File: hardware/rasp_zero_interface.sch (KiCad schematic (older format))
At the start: 0 parts

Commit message: work in progress - components ordered
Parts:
- added J2: Raspberry_Pi_2_3, Speeduino Mini:RaspberryPi_uHAT, symbol Connector:Raspberry_Pi_2_3
- added R23: 150, Resistors_SMD:R_0805, symbol Device:R
- added R24: 10k, Resistors_SMD:R_0805, symbol Device:R
- added U10, U5, U9: SN74LVC2T45-VSSOP, Housings_SSOP:VSSOP-8_2.3x2mm_Pitch0.5mm, symbol speeduino_mini:SN74LVC2T45-VSSOP
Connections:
- new net: J2.1 (3V3), J2.17 (3V3), R24.2, U10.8 (VCCB), U5.8 (VCCB), U9.8 (VCCB)
- new net: J2.10 (GPIO15/RXD), U10.6 (B2)
- new net: J2.12 (GPIO18/PWM0), U5.6 (B2)
- new net: J2.16 (GPIO23), R24.1, U9.7 (B1)
- new net: J2.18 (GPIO24), U10.7 (B1)
- new net: J2.8 (GPIO14/TXD), U5.7 (B1)
- new net: R23.1, U9.2 (A1)
- new net +5VA: J2.2 (5V), J2.4 (5V)
- new net +5VD: U10.1 (VCCA), U10.2 (A1), U10.5 (DIR), U5.1 (VCCA), U9.1 (VCCA)
- new net ATMEGA_RESET: R23.2
- new net GND: J2.14 (GND), J2.20 (GND), J2.25 (GND), J2.30 (GND), J2.34 (GND), J2.39 (GND), J2.6 (GND), J2.9 (GND), U10.4 (GND), U5.4 (GND), U5.5 (DIR), U9.4 (GND), U9.5 (DIR), U9.6 (B2)
- new net RXD_PDO: U10.3 (A2)
- new net SCK: U5.3 (A2)
- new net TXD_PDI: U5.2 (A1)
- no-connect marks 0 -> 23
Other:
- note added: "ATMEGA2561 ICSP Programming:\nGPIO14 - PDI\nGPIO15 - PDO\nGPIO18 - SCK\nGPIO23 - RST\nGPIO24 - VCC"
- note added: "Note: In order to program the ATMEGA2561 using the Raspberry PI, the Raspberry PI has to be self-powered.\nThis will also back-power all the sensors.\nMake sure to use a 2A power supply."

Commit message: rev 1
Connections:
- net +5VD: now also U10.7 (B1), U10.8 (VCCB); no longer U10.1 (VCCA), U10.2 (A1), U10.5 (DIR)
- net GND: now also U10.5 (DIR)
- net RXD_PDO: now also U10.6 (B2); no longer U10.3 (A2)
- net at J2.1 (3V3), J2.17 (3V3), R24.2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: now also U10.1 (VCCA); no longer U10.8 (VCCB)
- net at J2.10 (GPIO15/RXD): now also U10.3 (A2); no longer U10.6 (B2)
- net at J2.12 (GPIO18/PWM0): no longer U5.6 (B2)
- net at J2.18 (GPIO24): no longer U10.7 (B1)
- net at J2.31 (GCLK2/GPIO6): now also U10.2 (A1)
- net at J2.33 (PWM1/GPIO13): now also U5.6 (B2)
- no-connect marks 23 -> 24
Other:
- note added: "ATMEGA2561 ICSP Programming:\nGPIO14 - PDI\nGPIO15 - PDO\nGPIO13 - SCK\nGPIO23 - RST\nGPIO6 - VCC"
- note removed: "ATMEGA2561 ICSP Programming:\nGPIO14 - PDI\nGPIO15 - PDO\nGPIO18 - SCK\nGPIO23 - RST\nGPIO24 - VCC"
- note removed: "Note: In order to program the ATMEGA2561 using the Raspberry PI, the Raspberry PI has to be self-powered.\nThis will also back-power all the sensors.\nMake sure to use a 2A power supply."
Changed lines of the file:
@@
 EESchema Schematic File Version 4
 LIBS:speeduino_mini-cache
-EELAYER 26 0
+EELAYER 29 0
 EELAYER END
 $Descr A4 11693 8268
 encoding utf-8
-Sheet 18 18
+Sheet 18 21
 Title ""
 Date ""
@@
 F 4 "296-17014-1-ND" H 4200 6473 50  0000 C CNN "DIGIKEY"
 	1    4200 6150
-	1    0    0    -1
+	-1   0    0    -1
 $EndComp
 Wire Wire Line
@@
 Wire Wire Line
 	3700 3550 3700 3650
-Wire Wire Line
-	4600 6300 4600 6700
-Wire Wire Line
-	4600 6700 3550 6700
-Wire Wire Line
-	3550 6700 3550 6100
-Connection ~ 3550 6100
-Wire Wire Line
-	4600 3250 4700 3250
-Wire Wire Line
-	4700 3250 4700 3650
-Wire Wire Line
-	4700 3650 6350 3650
 Wire Wire Line
 	7250 2750 7250 2200
@@
 Text HLabel 2550 3250 0    50   Output ~ 0
 SCK
-Wire Wire Line
-	4600 6100 6100 6100
-Wire Wire Line
-	6100 6100 6100 4450
-Wire Wire Line
-	6100 4450 6350 4450
 Text Notes 6900 1850 0    50   ~ 0
-ATMEGA2561 ICSP Programming:\nGPIO14 - PDI\nGPIO15 - PDO\nGPIO18 - SCK\nGPIO23 - RST\nGPIO24 - VCC
+ATMEGA2561 ICSP Programming:\nGPIO14 - PDI\nGPIO15 - PDO\nGPIO13 - SCK\nGPIO23 - RST\nGPIO6 - VCC
 Wire Wire Line
 	5000 4350 6350 4350
@@
 NoConn ~ 6350 4650
 NoConn ~ 6350 4750
-NoConn ~ 7950 4850
 NoConn ~ 7950 4750
 NoConn ~ 7950 4550
@@
 NoConn ~ 7950 4350
 NoConn ~ 7950 4150
-NoConn ~ 7950 3950
+NoConn ~ 6350 4450
 NoConn ~ 7950 3850
 NoConn ~ 7950 3750
@@
 	0    1    1    0
 $EndComp
-Text Notes 1750 1700 0    50   ~ 0
-Note: In order to program the ATMEGA2561 using the Raspberry PI, the Raspberry PI has to be self-powered.\nThis will also back-power all the sensors.\nMake sure to use a 2A power supply.
 Connection ~ 4800 4250
 Wire Wire Line
@@
 Connection ~ 4600 4550
 NoConn ~ 6350 4550
+Wire Wire Line
+	8250 6100 8250 3950
+Wire Wire Line
+	8250 3950 7950 3950
+Wire Wire Line
+	4600 6100 8250 6100
+NoConn ~ 7950 4250
+NoConn ~ 6350 3650
+Wire Wire Line
+	7950 4850 8100 4850
+Wire Wire Line
+	8100 4850 8100 5900
+Wire Wire Line
+	8100 5900 5500 5900
+Wire Wire Line
+	5500 5900 5500 3250
+Wire Wire Line
+	4600 3250 5500 3250
+$Comp
+L power:GND #PWR0101
+U 1 1 5C8E8176
+P 4700 6400
+F 0 "#PWR0101" H 4700 6150 50  0001 C CNN
+F 1 "GND" H 4705 6227 50  0000 C CNN
+F 2 "" H 4700 6400 50  0001 C CNN
+F 3 "" H 4700 6400 50  0001 C CNN
+	1    4700 6400
+	1    0    0    -1
+$EndComp
+Wire Wire Line
+	4600 6300 4700 6300
+Wire Wire Line
+	4700 6300 4700 6400
 $EndSCHEMATC

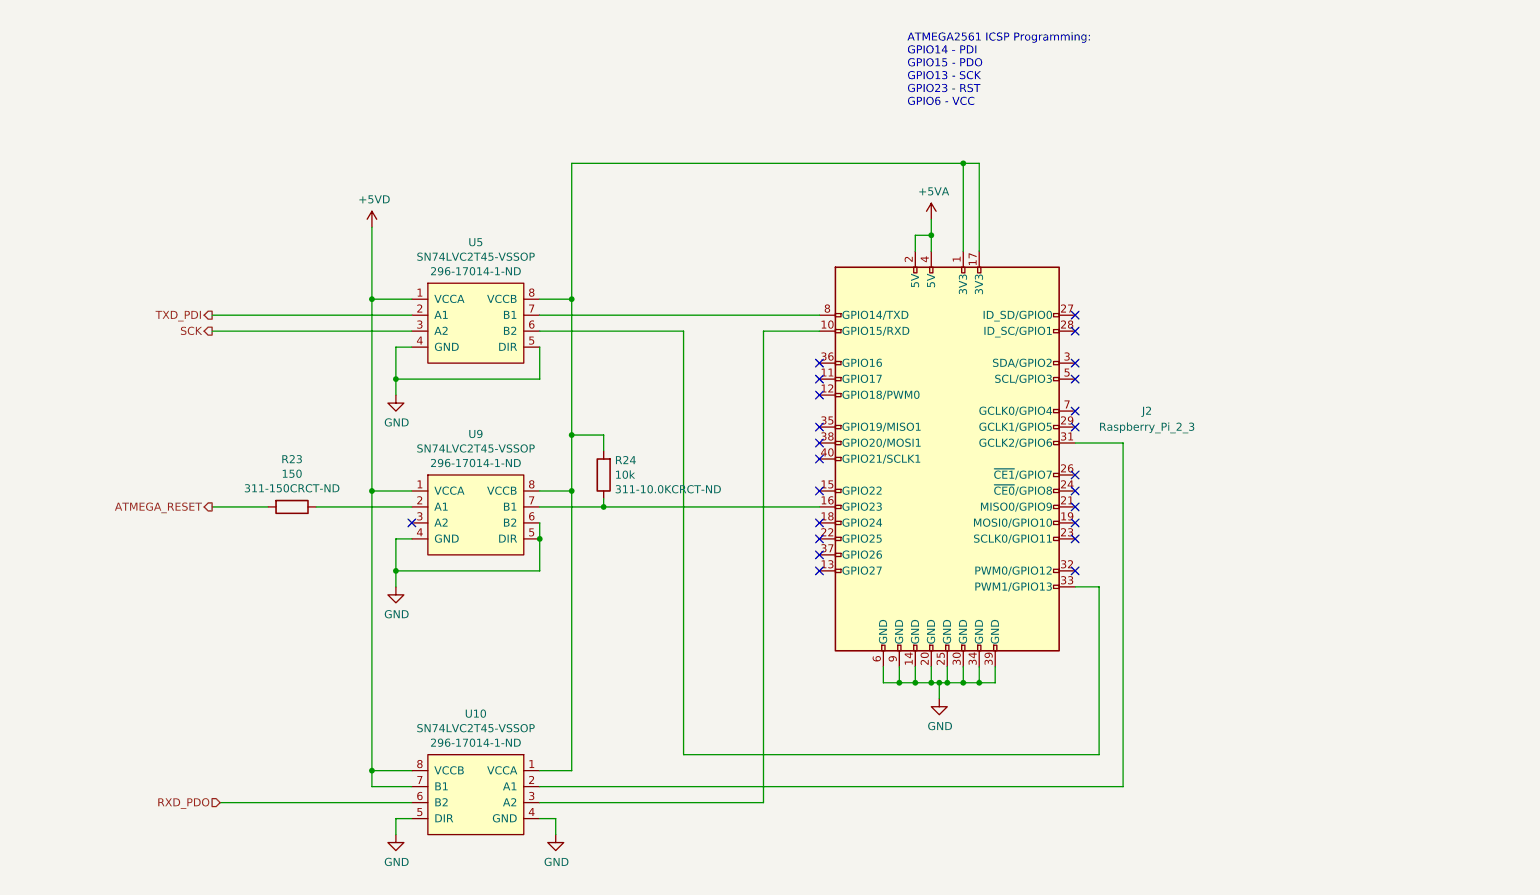
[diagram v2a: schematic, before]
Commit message: Adding corrections for wrong raspberry pi pinout
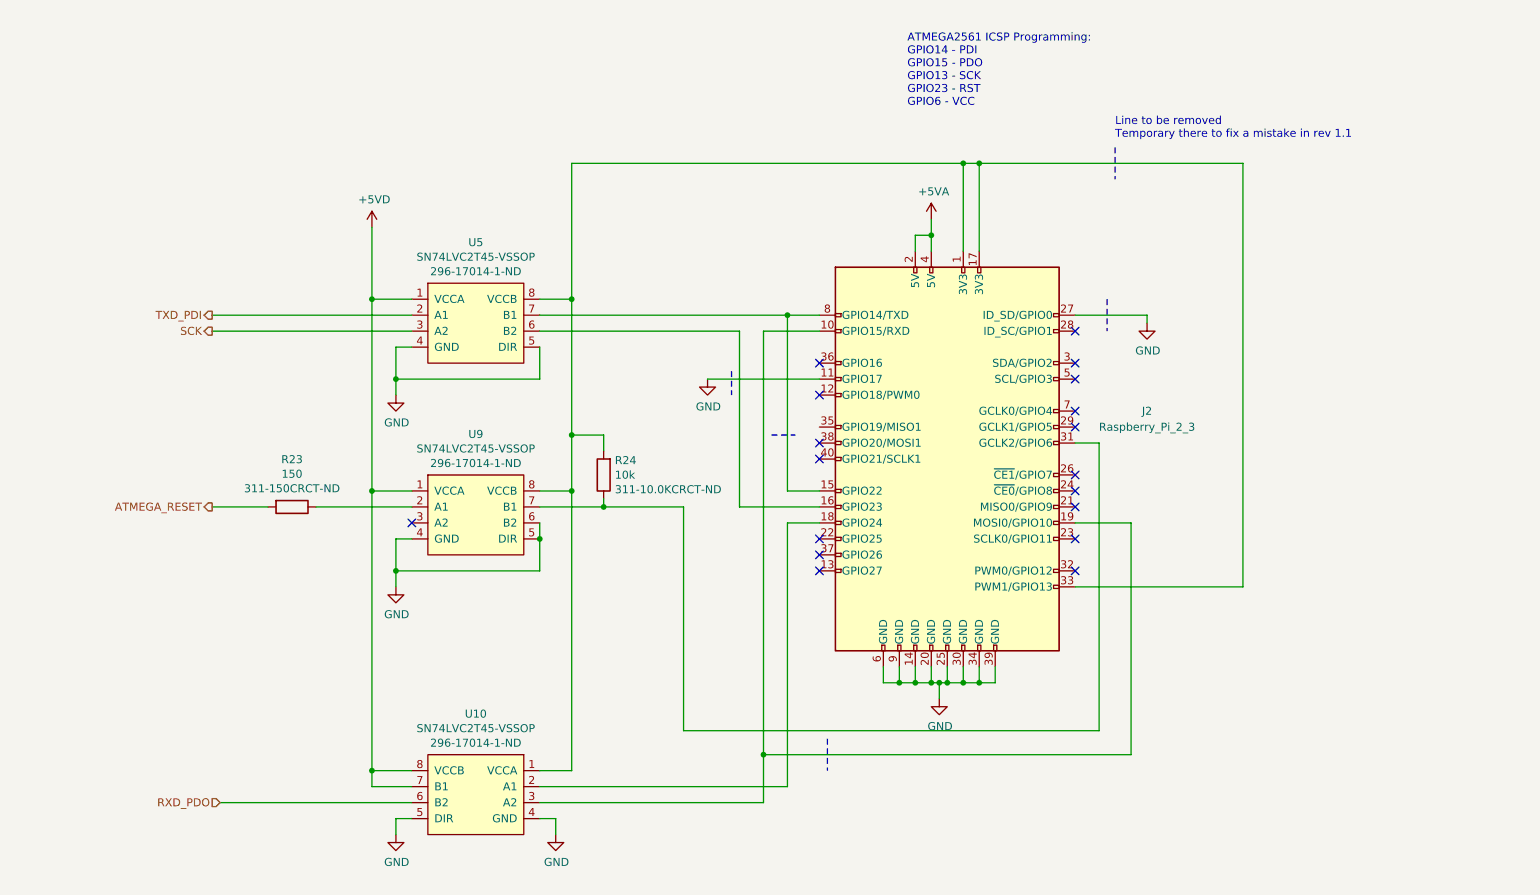
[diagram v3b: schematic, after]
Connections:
- net GND: now also J2.11 (GPIO17), J2.27 (ID_SD/GPIO0)
- net at J2.1 (3V3), J2.17 (3V3), R24.2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: now also J2.33 (PWM1/GPIO13)
- net at J2.10 (GPIO15/RXD), U10.3 (A2): now also J2.19 (MOSI0/GPIO10)
- net at J2.15 (GPIO22): now also J2.8 (GPIO14/TXD), U5.7 (B1)
- net at R24.1, U9.7 (B1): now also J2.31 (GCLK2/GPIO6); no longer J2.16 (GPIO23)
- net at J2.18 (GPIO24): now also U10.2 (A1)
- net at U5.6 (B2): now also J2.16 (GPIO23); no longer J2.33 (PWM1/GPIO13)
- no-connect marks 24 -> 18
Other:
- note added: "Line to be removed\nTemporary there to fix a mistake in rev 1.1"
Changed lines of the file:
@@
 $EndComp
 Wire Wire Line
-	6350 3150 4600 3150
+	6350 3150 6150 3150
 Wire Wire Line
 	4800 3050 4600 3050
@@
 Wire Wire Line
 	7050 2550 7050 2650
-Wire Wire Line
-	6000 3250 6000 6200
 Wire Wire Line
 	6000 6200 4600 6200
@@
 ATMEGA2561 ICSP Programming:\nGPIO14 - PDI\nGPIO15 - PDO\nGPIO13 - SCK\nGPIO23 - RST\nGPIO6 - VCC
 Wire Wire Line
-	5000 4350 6350 4350
-Wire Wire Line
 	5000 3900 4800 3900
 Connection ~ 4800 3900
@@
 	2900 4350 2550 4350
 NoConn ~ 6350 3450
-NoConn ~ 6350 3550
-NoConn ~ 6350 3850
 NoConn ~ 6350 3950
 NoConn ~ 6350 4050
-NoConn ~ 6350 4250
 NoConn ~ 6350 4650
 NoConn ~ 6350 4750
 NoConn ~ 7950 4750
 NoConn ~ 7950 4550
-NoConn ~ 7950 4450
 NoConn ~ 7950 4350
 NoConn ~ 7950 4150
-NoConn ~ 6350 4450
+NoConn ~ 6350 3650
 NoConn ~ 7950 3850
 NoConn ~ 7950 3750
@@
 NoConn ~ 7950 3450
 NoConn ~ 7950 3250
-NoConn ~ 7950 3150
 $Comp
 L Device:R R?
@@
 Wire Wire Line
 	4600 4350 5000 4350
-Connection ~ 5000 4350
 NoConn ~ 3800 4450
 Wire Wire Line
@@
 NoConn ~ 6350 4550
 Wire Wire Line
-	8250 6100 8250 3950
-Wire Wire Line
-	8250 3950 7950 3950
-Wire Wire Line
-	4600 6100 8250 6100
+	4600 6100 6150 6100
 NoConn ~ 7950 4250
-NoConn ~ 6350 3650
-Wire Wire Line
-	7950 4850 8100 4850
-Wire Wire Line
-	8100 4850 8100 5900
-Wire Wire Line
-	8100 5900 5500 5900
-Wire Wire Line
-	5500 5900 5500 3250
-Wire Wire Line
-	4600 3250 5500 3250
 $Comp
 L power:GND #PWR0101
@@
 Wire Wire Line
 	4700 6300 4700 6400
+Wire Wire Line
+	5000 4350 5500 4350
+Wire Wire Line
+	5500 4350 5500 5750
+Wire Wire Line
+	5500 5750 8100 5750
+Connection ~ 5000 4350
+Wire Wire Line
+	5850 3250 5850 4350
+Wire Wire Line
+	5850 4350 6350 4350
+Wire Wire Line
+	4600 3250 5850 3250
+Wire Wire Line
+	8100 3950 7950 3950
+Wire Wire Line
+	8100 3950 8100 5750
+Wire Wire Line
+	7350 2200 9000 2200
+Wire Wire Line
+	9000 2200 9000 4850
+Connection ~ 7350 2200
+Text Notes 8200 2050 0    50   ~ 0
+Line to be removed\nTemporary there to fix a mistake in rev 1.1
+$Comp
+L power:GND #PWR0106
+U 1 1 5CAFC06D
+P 8400 3200
+F 0 "#PWR0106" H 8400 2950 50  0001 C CNN
+F 1 "GND" H 8405 3027 50  0000 C CNN
+F 2 "" H 8400 3200 50  0001 C CNN
+F 3 "" H 8400 3200 50  0001 C CNN
+	1    8400 3200
+	1    0    0    -1
+$EndComp
+Wire Wire Line
+	7950 3150 8400 3150
+Wire Wire Line
+	8400 3150 8400 3200
+Wire Notes Line
+	8200 2100 8200 2300
+Wire Notes Line
+	8150 3050 8150 3250
+Wire Wire Line
+	6000 3250 6000 5900
+Wire Wire Line
+	9000 4850 7950 4850
+Wire Wire Line
+	7950 4450 8300 4450
+Wire Wire Line
+	8300 4450 8300 5900
+Wire Wire Line
+	8300 5900 6000 5900
+Connection ~ 6000 5900
+Wire Wire Line
+	6000 5900 6000 6200
+Wire Notes Line
+	6400 5800 6400 6000
+Wire Wire Line
+	6350 4450 6150 4450
+Wire Wire Line
+	6150 4450 6150 6100
+Wire Wire Line
+	6350 4250 6150 4250
+Wire Wire Line
+	6150 4250 6150 3150
+Connection ~ 6150 3150
+Wire Wire Line
+	6150 3150 4600 3150
+Wire Notes Line
+	6050 3900 6200 3900
+$Comp
+L power:GND #PWR0107
+U 1 1 5CB2CFEC
+P 5650 3550
+F 0 "#PWR0107" H 5650 3300 50  0001 C CNN
+F 1 "GND" H 5655 3377 50  0000 C CNN
+F 2 "" H 5650 3550 50  0001 C CNN
+F 3 "" H 5650 3550 50  0001 C CNN
+	1    5650 3550
+	1    0    0    -1
+$EndComp
+Wire Wire Line
+	5650 3550 6350 3550
+Wire Notes Line
+	5800 3500 5800 3650
 $EndSCHEMATC

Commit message: Rev 2 work in progress
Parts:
- added D2, D5: LED, LEDs:LED_0805_HandSoldering, symbol Device:LED
- added R31, R51: R_US, Resistors_SMD:R_0805_HandSoldering, symbol Device:R_US
- R23, R24: footprint Resistors_SMD:R_0805 -> Resistors_SMD:R_0805_HandSoldering; symbol Device:R -> Device:R_US
- U10, U5, U9: value SN74LVC2T45-VSSOP -> SN74LVC2T45MDCTTEP; footprint Housings_SSOP:VSSOP-8_2.3x2mm_Pitch0.5mm -> Housings_SSOP:SSOP-8_2.95x2.8mm_Pitch0.65mm; DIGIKEY 296-17014-1-ND -> 296-23952-1-ND
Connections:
- net GND: now also D2.1 (K), D5.1 (K); no longer J2.11 (GPIO17), J2.27 (ID_SD/GPIO0)
- net at J2.1 (3V3), J2.17 (3V3), R24.2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: no longer J2.33 (PWM1/GPIO13)
- net at J2.10 (GPIO15/RXD), U10.3 (A2): no longer J2.19 (MOSI0/GPIO10)
- net at J2.8 (GPIO14/TXD), U5.7 (B1): no longer J2.15 (GPIO22)
- net at J2.16 (GPIO23): now also R24.1, U9.7 (B1); no longer U5.6 (B2)
- net at J2.18 (GPIO24): no longer U10.2 (A1)
- net at J2.32 (PWM0/GPIO12): now also R51.2
- net at J2.7 (GCLK0/GPIO4): now also U5.6 (B2)
- new net: J2.33 (PWM1/GPIO13), R31.2
- new net: D2.2 (A), R31.1
- new net: D5.2 (A), R51.1
- now unconnected: J2.31 (GCLK2/GPIO6)
- no-connect marks 18 -> 16
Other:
- note removed: "Line to be removed\nTemporary there to fix a mistake in rev 1.1"
- moved on the sheet: J2, U5

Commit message: hardware rev2 - layout complete
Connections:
- net GND: no longer J2.25 (GND), J2.39 (GND), J2.9 (GND)
- no-connect marks 16 -> 19
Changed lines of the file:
@@
 	6200 5250 6200 5350
 Wire Wire Line
-	6200 5350 6300 5350
-Wire Wire Line
 	6550 5350 6550 5450
-Wire Wire Line
-	6550 5350 6600 5350
-Wire Wire Line
-	6900 5350 6900 5250
 Connection ~ 6550 5350
 Wire Wire Line
 	6800 5250 6800 5350
-Connection ~ 6800 5350
-Wire Wire Line
-	6800 5350 6900 5350
 Wire Wire Line
 	6700 5250 6700 5350
@@
 	6700 5350 6800 5350
 Wire Wire Line
-	6600 5250 6600 5350
-Connection ~ 6600 5350
-Wire Wire Line
-	6600 5350 6700 5350
-Wire Wire Line
 	6500 5250 6500 5350
 Connection ~ 6500 5350
@@
 Wire Wire Line
 	6400 5350 6500 5350
-Wire Wire Line
-	6300 5250 6300 5350
-Connection ~ 6300 5350
-Wire Wire Line
-	6300 5350 6400 5350
 Text HLabel 2000 4250 0    50   Output ~ 0
 ATMEGA_RESET
@@
 Wire Wire Line
 	8300 4650 8300 4950
+Wire Wire Line
+	6200 5350 6400 5350
+NoConn ~ 6300 5250
+Wire Wire Line
+	6550 5350 6700 5350
+NoConn ~ 6600 5250
+NoConn ~ 6900 5250
 $EndSCHEMATC

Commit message: rev 2 sent to fab
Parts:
- D2: value LED -> LED BLUE 10mA 3V; DigiKey (none) -> 732-4982-1-ND
- D5: value LED -> LED RED 10mA 1.9V; DigiKey (none) -> 732-4984-1-ND
- J2: DigiKey (none) -> S7123-ND
- R23: DIGIKEY 311-150CRCT-ND -> (none); DigiKey (none) -> 311-150CRCT-ND
- R24: DIGIKEY 311-10.0KCRCT-ND -> (none); DigiKey (none) -> 311-10.0KCRCT-ND
- R31: value R_US -> 200; DigiKey (none) -> P200CCT-ND
- R51: value R_US -> 309; DigiKey (none) -> P309CCT-ND
- U10, U5, U9: DIGIKEY 296-23952-1-ND -> (none); DigiKey (none) -> 296-23952-1-ND
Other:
- note added: "Pin header male pins: DigiKey part S2011E-20-ND\nStandoffs: 4x 1772-1705-ND\nScrews: 8x 1772-1467-ND"
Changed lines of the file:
@@
 F 2 "Speeduino Mini:RaspberryPi_uHAT" H 6600 3950 50  0001 C CNN
 F 3 "https://www.raspberrypi.org/documentation/hardware/raspberrypi/schematics/rpi_SCH_3bplus_1p0_reduced.pdf" H 6600 3950 50  0001 C CNN
+F 4 "S7123-ND" H 0   0   50  0001 C CNN "DigiKey"
 	1    6600 3950
 	1    0    0    -1
@@
 F 2 "Housings_SSOP:SSOP-8_2.95x2.8mm_Pitch0.65mm" H 3650 2500 50  0001 C CNN
 F 3 "http://www.ti.com/lit/ds/symlink/sn74lvc2t45-ep.pdf" H 3650 2400 50  0001 C CNN
-F 4 "296-23952-1-ND" H 3650 3423 50  0000 C CNN "DIGIKEY"
+F 4 "296-23952-1-ND" H 0   0   50  0001 C CNN "DigiKey"
 	1    3650 3100
 	1    0    0    -1
@@
 AR Path="/5C838946" Ref="R?"  Part="1"
 AR Path="/5C6B9F28/5C838946" Ref="R24"  Part="1"
-F 0 "R24" H 4380 3959 50  0000 R CNN
-F 1 "10k" H 4380 4050 50  0000 R CNN
+F 0 "R24" H 4382 3959 50  0000 R CNN
+F 1 "10k" H 4382 4050 50  0000 R CNN
 F 2 "Resistors_SMD:R_0805_HandSoldering" V 4380 4050 50  0001 C CNN
 F 3 "~" H 4450 4050 50  0001 C CNN
-F 4 "311-10.0KCRCT-ND" H 4380 4141 50  0000 R CNN "DIGIKEY"
+F 4 "311-10.0KCRCT-ND" H 4382 4141 50  0000 R CNN "DigiKey"
 	1    4450 4050
 	-1   0    0    1
@@
 AR Path="/5C668FC1/5C83C8E7" Ref="R?"  Part="1"
 AR Path="/5C6B9F28/5C83C8E7" Ref="R23"  Part="1"
-F 0 "R23" V 2203 4250 50  0000 C CNN
-F 1 "150" V 2294 4250 50  0000 C CNN
+F 0 "R23" V 2205 4250 50  0000 C CNN
+F 1 "150" V 2296 4250 50  0000 C CNN
 F 2 "Resistors_SMD:R_0805_HandSoldering" V 2430 4250 50  0001 C CNN
 F 3 "~" H 2500 4250 50  0001 C CNN
-F 4 "311-150CRCT-ND" V 2385 4250 50  0000 C CNN "DIGIKEY"
+F 4 "311-150CRCT-ND" V 2387 4250 50  0000 C CNN "DigiKey"
 	1    2500 4250
 	0    1    1    0
@@
 F 2 "Housings_SSOP:SSOP-8_2.95x2.8mm_Pitch0.65mm" H 3650 3700 50  0001 C CNN
 F 3 "http://www.ti.com/lit/ds/symlink/sn74lvc2t45-ep.pdf" H 3650 3600 50  0001 C CNN
-F 4 "296-23952-1-ND" H 3650 4623 50  0000 C CNN "DIGIKEY"
+F 4 "296-23952-1-ND" H 0   0   50  0001 C CNN "DigiKey"
 	1    3650 4300
 	1    0    0    -1
@@
 F 2 "Housings_SSOP:SSOP-8_2.95x2.8mm_Pitch0.65mm" H 3650 5450 50  0001 C CNN
 F 3 "http://www.ti.com/lit/ds/symlink/sn74lvc2t45-ep.pdf" H 3650 5350 50  0001 C CNN
-F 4 "296-23952-1-ND" H 3650 6373 50  0000 C CNN "DIGIKEY"
+F 4 "296-23952-1-ND" H 0   0   50  0001 C CNN "DigiKey"
 	1    3650 6050
 	-1   0    0    -1
@@
 AR Path="/5C95BECF/5D461AF2" Ref="D?"  Part="1"
 AR Path="/5C6B9F28/5D461AF2" Ref="D2"  Part="1"
-F 0 "D2" V 7839 5383 50  0000 R CNN
-F 1 "LED" V 7748 5383 50  0000 R CNN
+F 0 "D2" V 7884 5579 50  0000 L CNN
+F 1 "LED BLUE 10mA 3V" V 7793 5579 50  0000 L CNN
 F 2 "LEDs:LED_0805_HandSoldering" H 7800 5500 50  0001 C CNN
 F 3 "~" H 7800 5500 50  0001 C CNN
+F 4 "732-4982-1-ND" V 7702 5579 50  0000 L CNN "DigiKey"
 	1    7800 5500
 	0    -1   -1   0
@@
 AR Path="/5C6B9F28/5D461AF8" Ref="R31"  Part="1"
 F 0 "R31" H 7732 5054 50  0000 R CNN
-F 1 "R_US" H 7732 5145 50  0000 R CNN
+F 1 "200" H 7732 5145 50  0000 R CNN
 F 2 "Resistors_SMD:R_0805_HandSoldering" V 7840 5090 50  0001 C CNN
 F 3 "~" H 7800 5100 50  0001 C CNN
+F 4 "P200CCT-ND" H 0   0   50  0001 C CNN "DigiKey"
 	1    7800 5100
 	-1   0    0    1
@@
 AR Path="/5C95BECF/5D4692B0" Ref="D?"  Part="1"
 AR Path="/5C6B9F28/5D4692B0" Ref="D5"  Part="1"
-F 0 "D5" V 8339 5383 50  0000 R CNN
-F 1 "LED" V 8248 5383 50  0000 R CNN
+F 0 "D5" V 8384 5383 50  0000 R CNN
+F 1 "LED RED 10mA 1.9V" V 8293 5383 50  0000 R CNN
 F 2 "LEDs:LED_0805_HandSoldering" H 8300 5500 50  0001 C CNN
 F 3 "~" H 8300 5500 50  0001 C CNN
+F 4 "732-4984-1-ND" V 8202 5383 50  0000 R CNN "DigiKey"
 	1    8300 5500
 	0    -1   -1   0
@@
 AR Path="/5C6B9F28/5D4692BA" Ref="R51"  Part="1"
 F 0 "R51" H 8232 5054 50  0000 R CNN
-F 1 "R_US" H 8232 5145 50  0000 R CNN
+F 1 "309" H 8232 5145 50  0000 R CNN
 F 2 "Resistors_SMD:R_0805_HandSoldering" V 8340 5090 50  0001 C CNN
 F 3 "~" H 8300 5100 50  0001 C CNN
+F 4 "P309CCT-ND" H 0   0   50  0001 C CNN "DigiKey"
 	1    8300 5100
 	-1   0    0    1
@@
 NoConn ~ 6600 5250
 NoConn ~ 6900 5250
+Text Notes 8450 4250 0    50   ~ 0
+Pin header male pins: DigiKey part S2011E-20-ND\nStandoffs:  4x 1772-1705-ND\nScrews: 8x 1772-1467-ND
 $EndSCHEMATC
